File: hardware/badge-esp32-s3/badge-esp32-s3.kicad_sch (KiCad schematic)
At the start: 4 parts, among them U1 ESP32-S3-MINI-1-N8

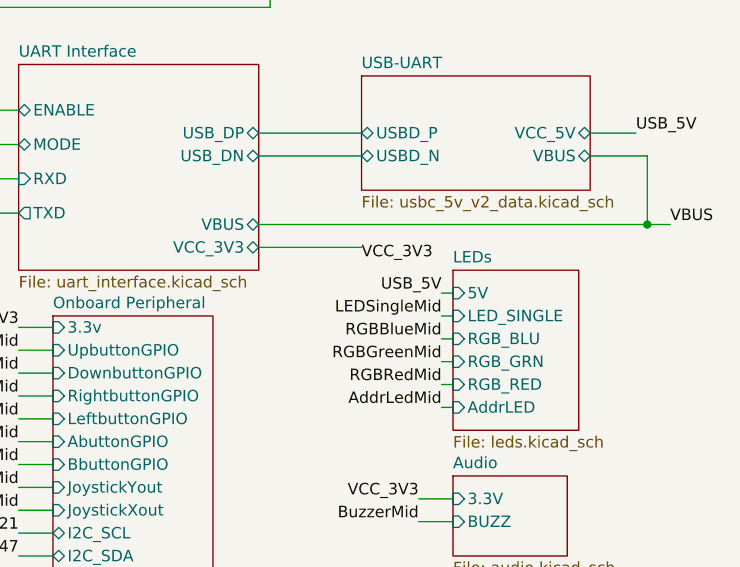
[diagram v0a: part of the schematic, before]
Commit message: Updated the wiring for the 5V line to be connected to the +4V net. That is what it is named even though it is 4.5 ish volts.
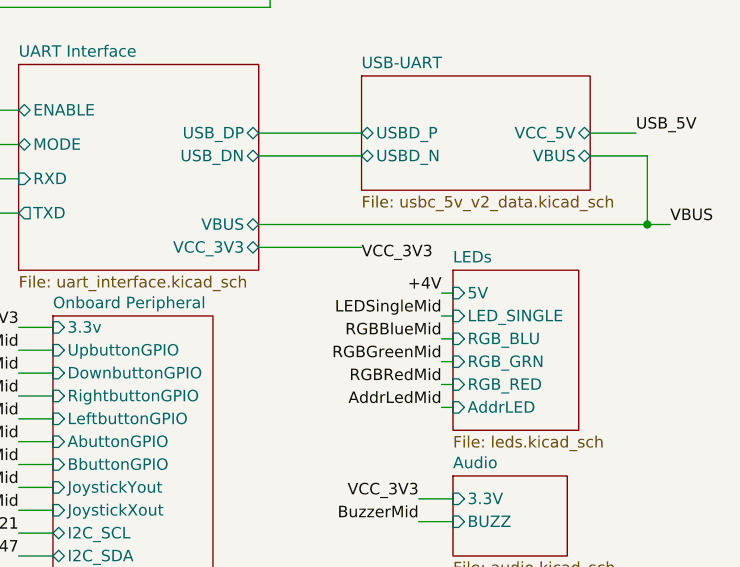
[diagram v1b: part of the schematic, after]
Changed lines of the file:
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@@
 		)
 	)
-	(label "USB_5V"
+	(label "+4V"
 		(at 254 64.77 180)
 		(effects

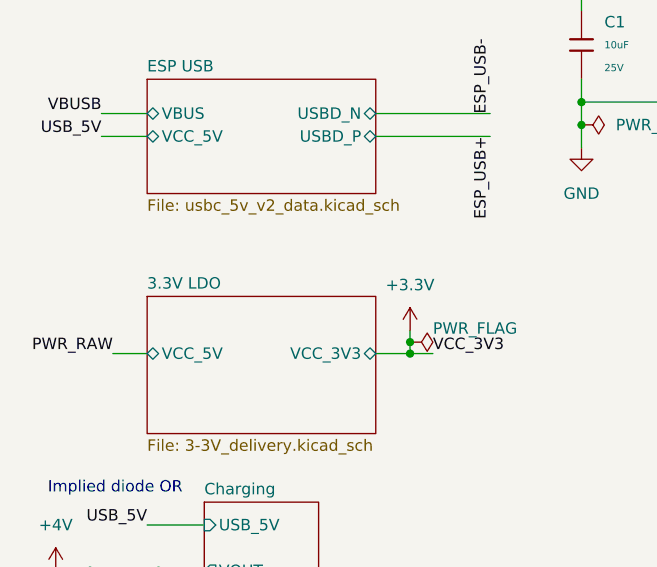
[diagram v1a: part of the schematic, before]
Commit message: Started adding the circuitry for the 5V voltage booster.
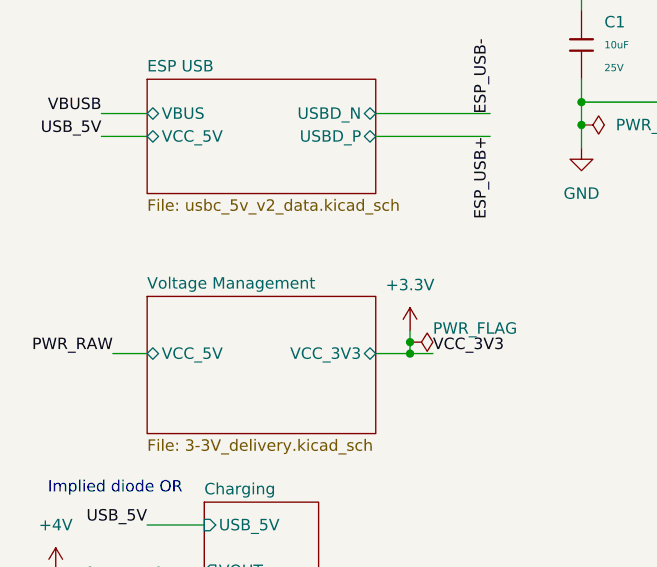
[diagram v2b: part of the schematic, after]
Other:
- sheet 3.3V LDO renamed Voltage Management
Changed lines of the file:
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@@
 			(color 0 0 0 0.0000)
 		)
-		(property "Sheetname" "3.3V LDO"
+		(property "Sheetname" "Voltage Management"
 			(at 25.4 69.1384 0)
 			(effects

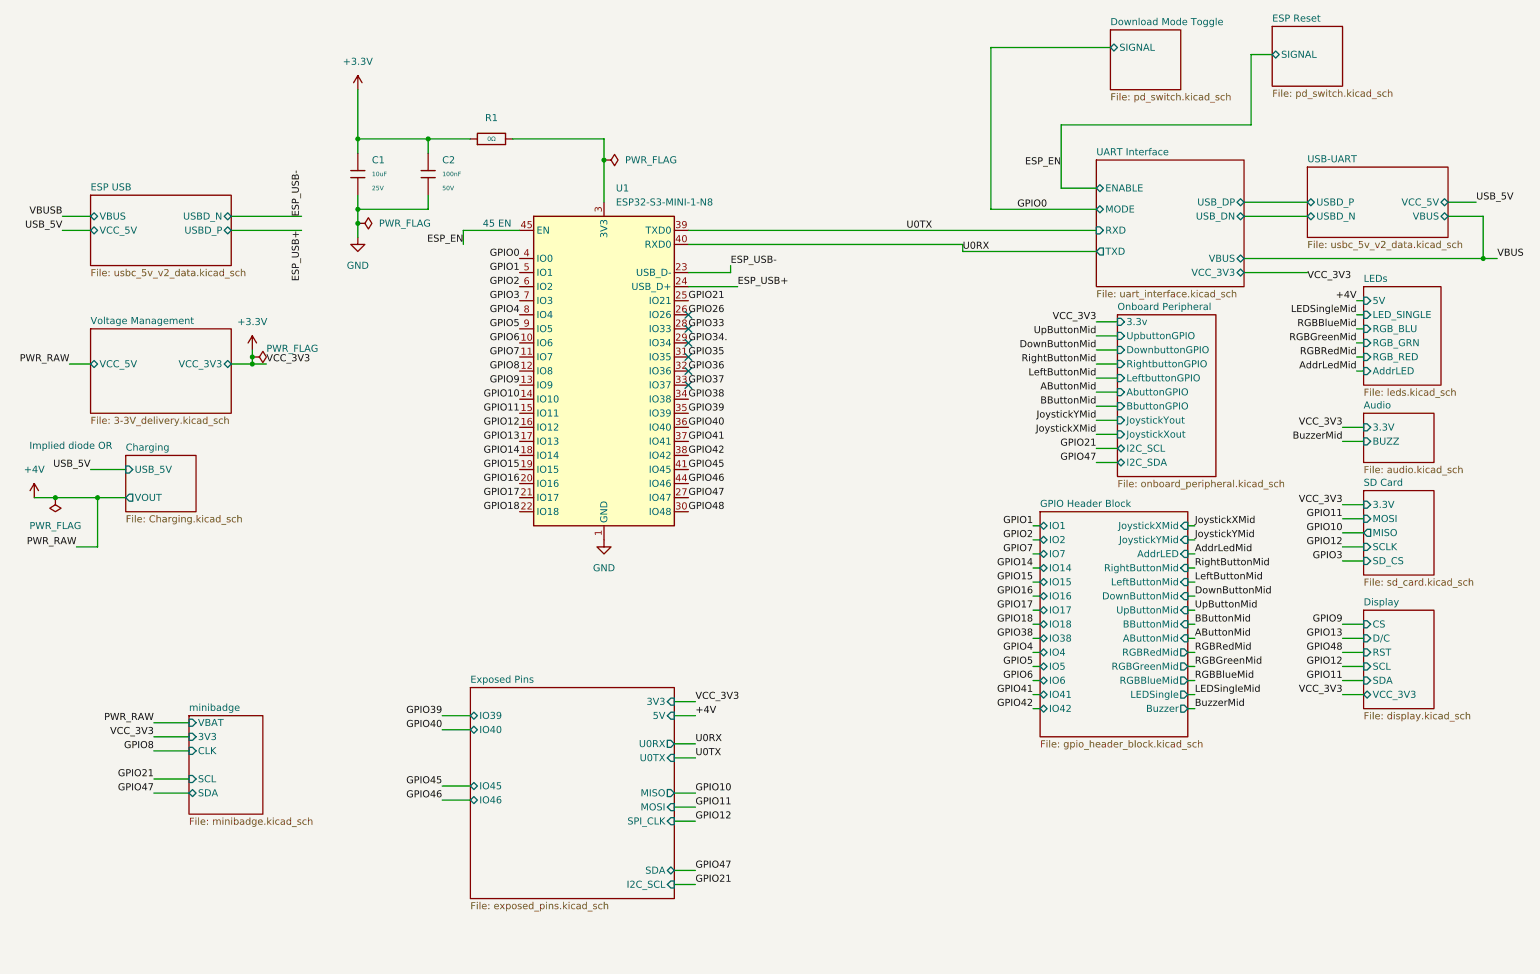
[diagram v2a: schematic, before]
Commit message: Added the buck-boost converter. The traces aren't all connected though.
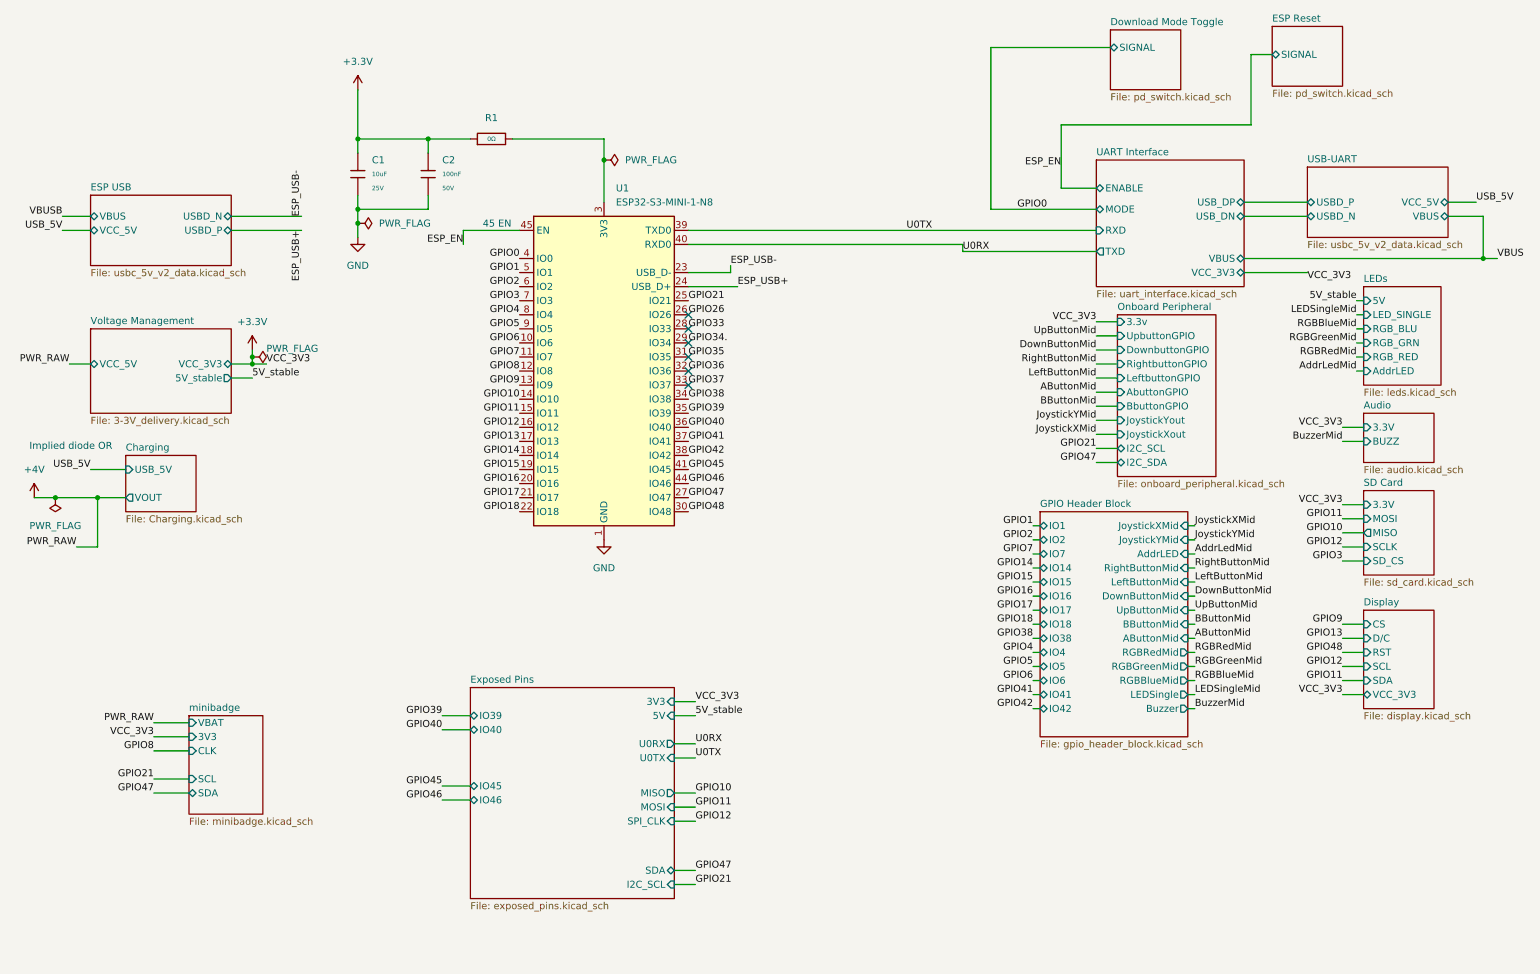
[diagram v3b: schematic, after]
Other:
- sheet Voltage Management ports: added 5V_stable; removed none
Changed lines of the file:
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@@
 	(wire
 		(pts
+			(xy 50.8 78.74) (xy 54.61 78.74)
+		)
+		(stroke
+			(width 0)
+			(type default)
+		)
+	)
+	(wire
+		(pts
 			(xy 54.61 76.2) (xy 57.15 76.2)
 		)
@@
 		)
 	)
-	(label "+4V"
+	(label "5V_stable"
 		(at 254 64.77 180)
 		(effects
@@
 		)
 	)
-	(label "+4V"
+	(label "5V_stable"
 		(at 134.62 139.7 0)
 		(effects
@@
 		)
 	)
+	(label "5V_stable"
+		(at 54.61 78.74 0)
+		(effects
+			(font
+				(size 1.27 1.27)
+			)
+			(justify left bottom)
+		)
+	)
 	(label "PWR_RAW"
 		(at 22.86 109.22 180)
@@
 			)
 		)
+		(pin "5V_stable" output
+			(at 50.8 78.74 0)
+			(effects
+				(font
+					(size 1.27 1.27)
+				)
+				(justify right)
+			)
+		)

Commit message: ESP32-S3_mini-1-N4R2
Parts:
- U1: value ESP32-S3-MINI-1-N8 -> ESP32-S3-MINI-1-N4R2; LCSC Part C2913206 -> C3013941
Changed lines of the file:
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@@
 			)
 		)
-		(property "Value" "ESP32-S3-MINI-1-N8"
+		(property "Value" "ESP32-S3-MINI-1-N4R2"
 			(at 120.2533 46.99 0)
 			(effects
@@
 			)
 		)
-		(property "LCSC Part" "C2913206"
+		(property "LCSC Part" "C3013941"
 			(at 118.11 77.47 0)
 			(effects

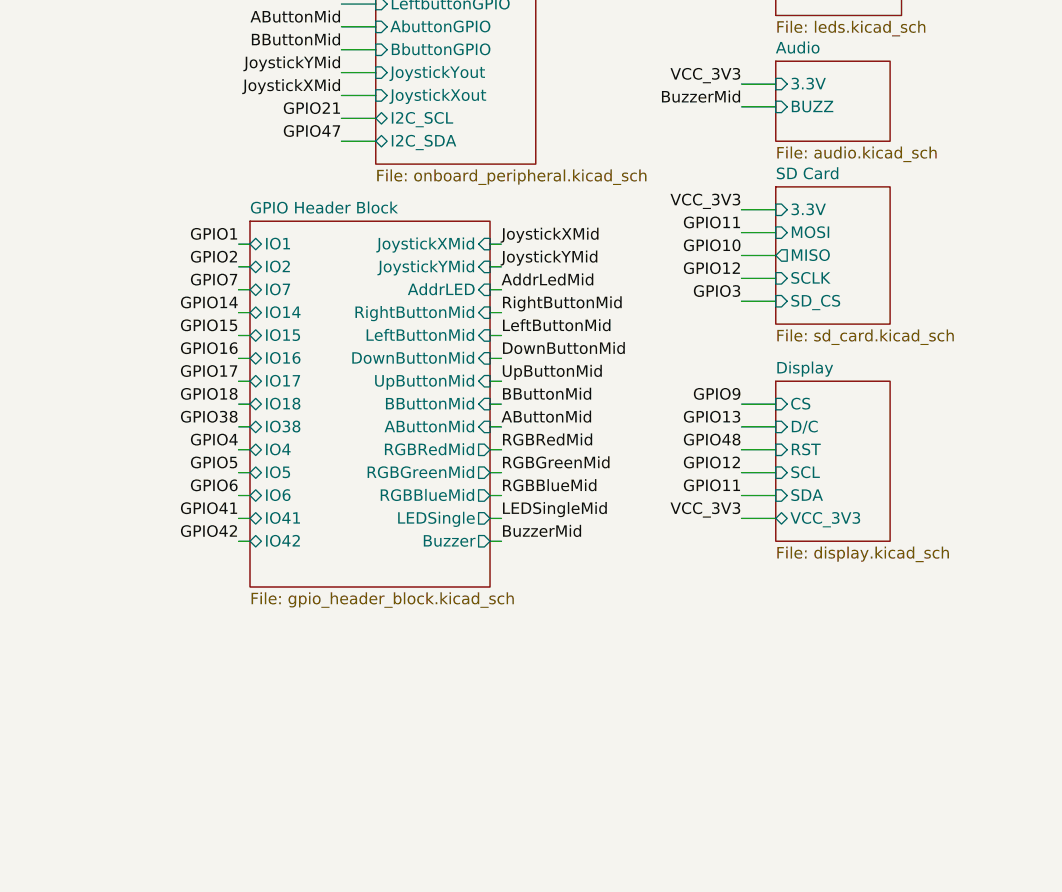
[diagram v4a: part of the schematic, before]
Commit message: added sdio
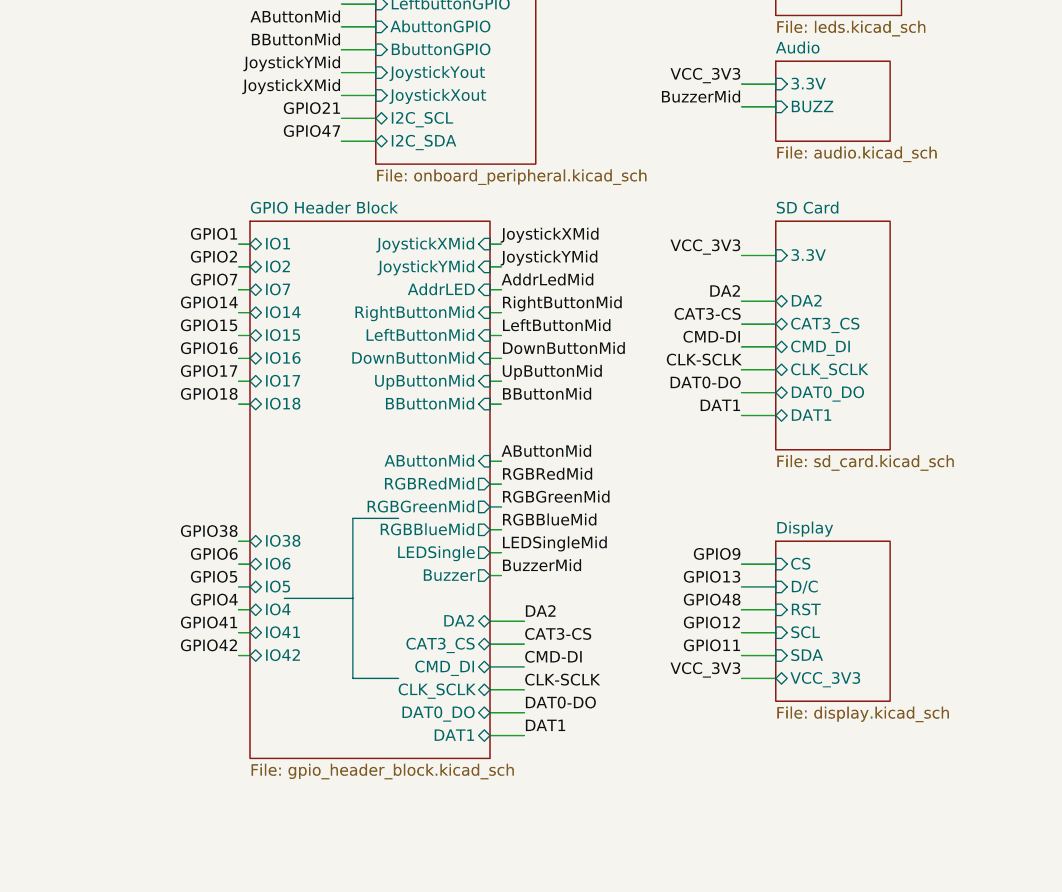
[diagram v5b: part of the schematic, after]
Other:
- sheet GPIO Header Block ports: added CAT3_CS, CLK_SCLK, CMD_DI, DA2, DAT0_DO, DAT1; removed none
- sheet SD Card ports: added CAT3_CS, CLK_SCLK, CMD_DI, DA2, DAT0_DO, DAT1; removed MISO, MOSI, SCLK, SD_CS

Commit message: almost finished
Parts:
- added H1, H2, H3, H4: MountingHole, MountingHole_3.2mm_M3_ISO7380_Pad_TopBottom, symbol Mechanical:MountingHole
- added H5: MountingHole, MountingHole:MountingHole_5.3mm_M5, symbol Mechanical:MountingHole
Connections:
- net +3.3V: now also R1.2; no longer C1.1, C2.1, R1.1
- net at U1.3 (3V3): now also C1.1, C2.1, R1.1; no longer R1.2
- net GPIO34. renamed GPIO34
- no-connect marks 6 -> 1
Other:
- sheet Audio ports: added 3.3v; removed 3.3V
- sheet Charging ports: added VBATT; removed none
- sheet Exposed Pins ports: added SPI_MISO, SPI_MOSI, U1RX, U1TX; removed IO39, IO40, MISO, MOSI
- sheet GPIO Header Block ports: added BatteryVoltage, IO43; removed CAT3_CS, CLK_SCLK, CMD_DI, DA2, DAT0_DO, DAT1
- sheet LEDs ports: added LED_SINGLE1; removed LED_SINGLE
- sheet SD Card ports: added 3.3v, MISO, MOSI, SCLK, SD_CS; removed 3.3V, CAT3_CS, CLK_SCLK, CMD_DI, DA2, DAT0_DO, DAT1
- sheet Voltage Management ports: added VBATT, V_Sense; removed none
- sheet minibadge ports: added B1CLK, B1IO1, B1IO2, B2CLK, B2IO1, B2IO2; removed CLK
- moved on the sheet: R1
